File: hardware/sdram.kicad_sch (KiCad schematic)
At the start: 2 parts, among them U1 ECP5U_12_CABGA256, U7 W9825G6KH

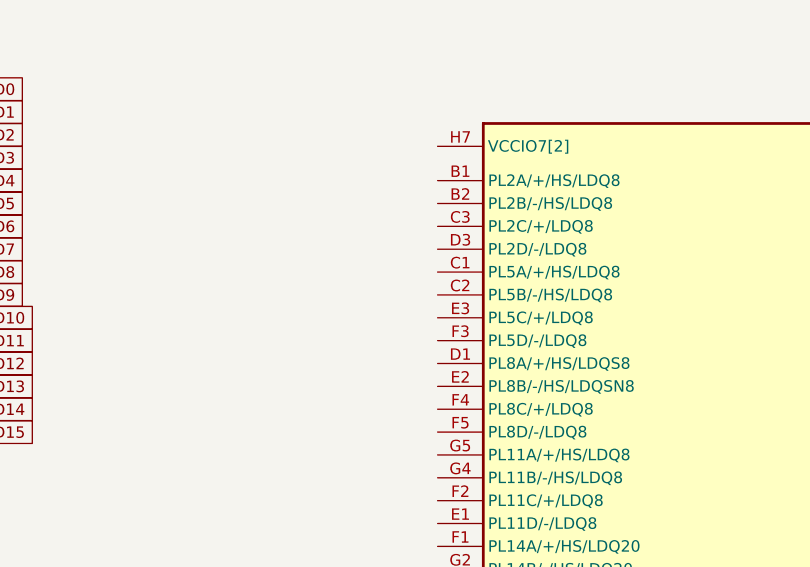
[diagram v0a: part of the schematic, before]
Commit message: Routed most of sdram
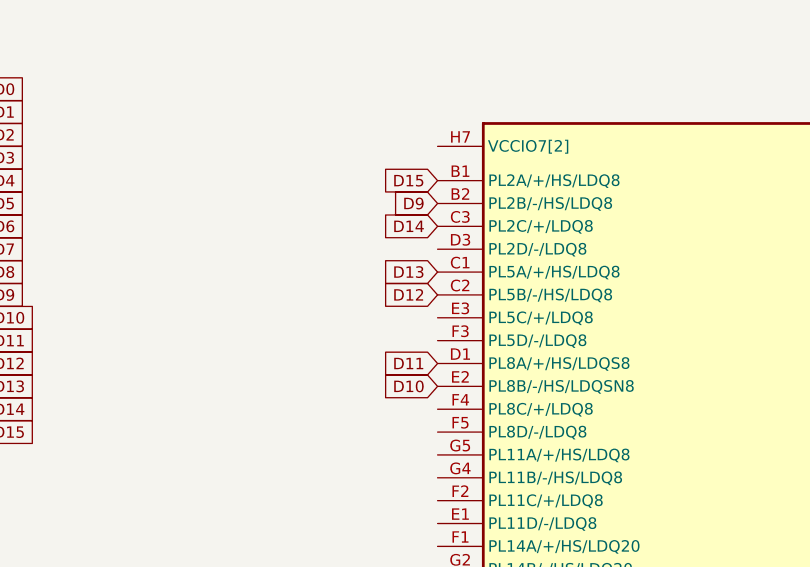
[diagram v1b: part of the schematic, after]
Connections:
- net D10: now also U1.E2 (PL8B/-/HS/LDQSN8)
- net D11: now also U1.D1 (PL8A/+/HS/LDQS8)
- net D12: now also U1.C2 (PL5B/-/HS/LDQ8)
- net D13: now also U1.C1 (PL5A/+/HS/LDQ8)
- net D14: now also U1.C3 (PL2C/+/LDQ8)
- net D15: now also U1.B1 (PL2A/+/HS/LDQ8)
- net D9: now also U1.B2 (PL2B/-/HS/LDQ8)
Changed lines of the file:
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@@
+		)
+	)
+	(global_label "D13"
+		(shape input)
+		(at 113.03 58.42 180)
+		(fields_autoplaced yes)
+		(effects
+			(font
+				(size 1.27 1.27)
+			)
+			(justify right)
+		)
+		(property "Intersheetrefs" "${INTERSHEET_REFS}"
+			(at 106.3558 58.42 0)
+			(effects
+				(font
+					(size 1.27 1.27)
+				)
+				(justify right)
+				(hide yes)
+			)
 		)
 	)
@@
 		)
 	)
+	(global_label "D9"
+		(shape input)
+		(at 113.03 50.8 180)
+		(fields_autoplaced yes)
+		(effects
+			(font
+				(size 1.27 1.27)
+			)
+			(justify right)
+		)
+		(property "Intersheetrefs" "${INTERSHEET_REFS}"
+			(at 107.5653 50.8 0)
+			(effects
+				(font
+					(size 1.27 1.27)
+				)
+				(justify right)
+				(hide yes)
+			)
+		)
+	)
 	(global_label "DQM1"
 		(shape input)
@@
 		)
 	)
+	(global_label "D14"
+		(shape input)
+		(at 113.03 53.34 180)
+		(fields_autoplaced yes)
+		(effects
+			(font
+				(size 1.27 1.27)
+			)
+			(justify right)
+		)
+		(property "Intersheetrefs" "${INTERSHEET_REFS}"
+			(at 106.3558 53.34 0)
+			(effects
+				(font
+					(size 1.27 1.27)
+				)
+				(justify right)
+				(hide yes)
+			)
+		)
+	)
+	(global_label "D10"
+		(shape input)
+		(at 113.03 71.12 180)
+		(fields_autoplaced yes)
+		(effects
+			(font
+				(size 1.27 1.27)
+			)
+			(justify right)
+		)
+		(property "Intersheetrefs" "${INTERSHEET_REFS}"
+			(at 106.3558 71.12 0)
+			(effects
+				(font
+					(size 1.27 1.27)
+				)
+				(justify right)
+				(hide yes)
+			)
+		)
+	)
+	(global_label "D15"
+		(shape input)
+		(at 113.03 48.26 180)
+		(fields_autoplaced yes)
+		(effects
+			(font
+				(size 1.27 1.27)
+			)
+			(justify right)
+		)
+		(property "Intersheetrefs" "${INTERSHEET_REFS}"
+			(at 106.3558 48.26 0)
+			(effects
+				(font
+					(size 1.27 1.27)
+				)
+				(justify right)
+				(hide yes)
+			)
+		)
+	)
 	(global_label "D2"
 		(shape input)
@@
 		)
 	)
+	(global_label "D11"
+		(shape input)
+		(at 113.03 68.58 180)
+		(fields_autoplaced yes)
+		(effects
+			(font
+				(size 1.27 1.27)
+			)
+			(justify right)
+		)
+		(property "Intersheetrefs" "${INTERSHEET_REFS}"
+			(at 106.3558 68.58 0)
+			(effects
+				(font
+					(size 1.27 1.27)
+				)
+				(justify right)
+				(hide yes)
+			)
+		)
+	)
 	(global_label "A10"
 		(shape input)
@@
 		(property "Intersheetrefs" "${INTERSHEET_REFS}"
 			(at 31.5467 48.26 0)
+			(effects
+				(font
+					(size 1.27 1.27)
+				)
+				(justify right)
+				(hide yes)
+			)
+		)
+	)
+	(global_label "D12"
+		(shape input)
+		(at 113.03 60.96 180)
+		(fields_autoplaced yes)
+		(effects
+			(font
+				(size 1.27 1.27)
+			)
+			(justify right)
+		)
+		(property "Intersheetrefs" "${INTERSHEET_REFS}"
+			(at 106.3558 60.96 0)
 			(effects
 				(font
@@
 			)
 		)
-		(property "Datasheet" ""
+		(property "Datasheet" "https://www.lcsc.com/datasheet/lcsc_datasheet_2411220131_Lattice-LFE5U-25F-6BG256C_C1521614.pdf"
 			(at 116.84 43.18 0)
 			(effects

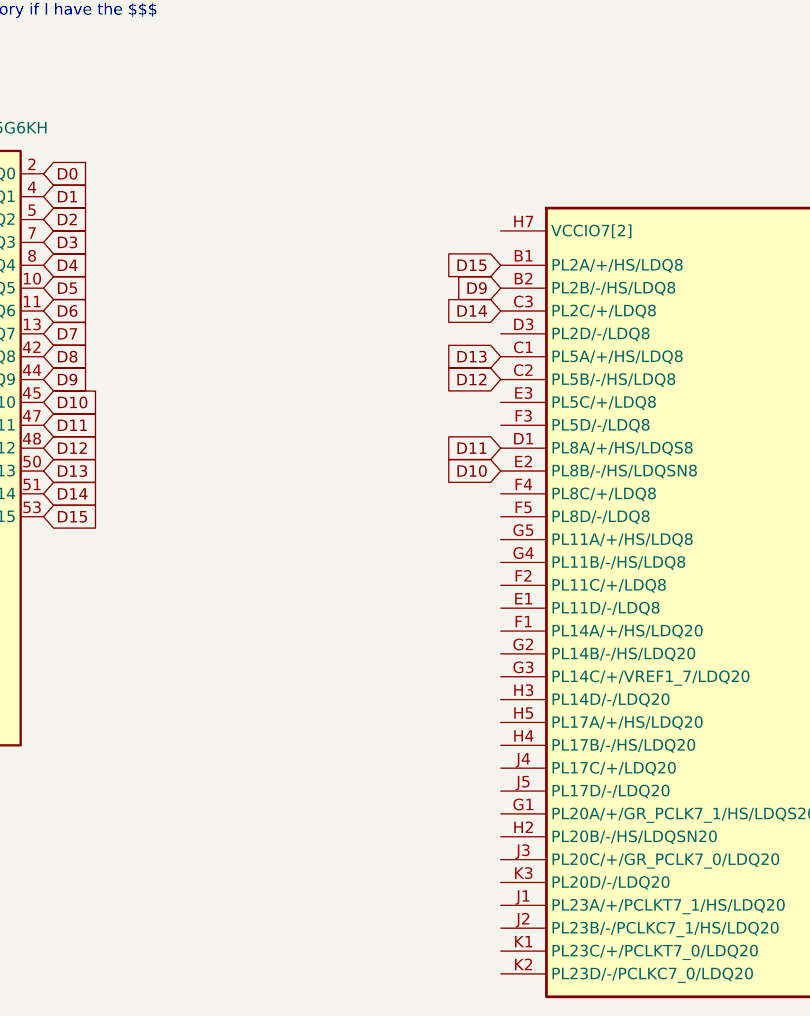
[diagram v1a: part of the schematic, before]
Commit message: Added the decoupling capacitors
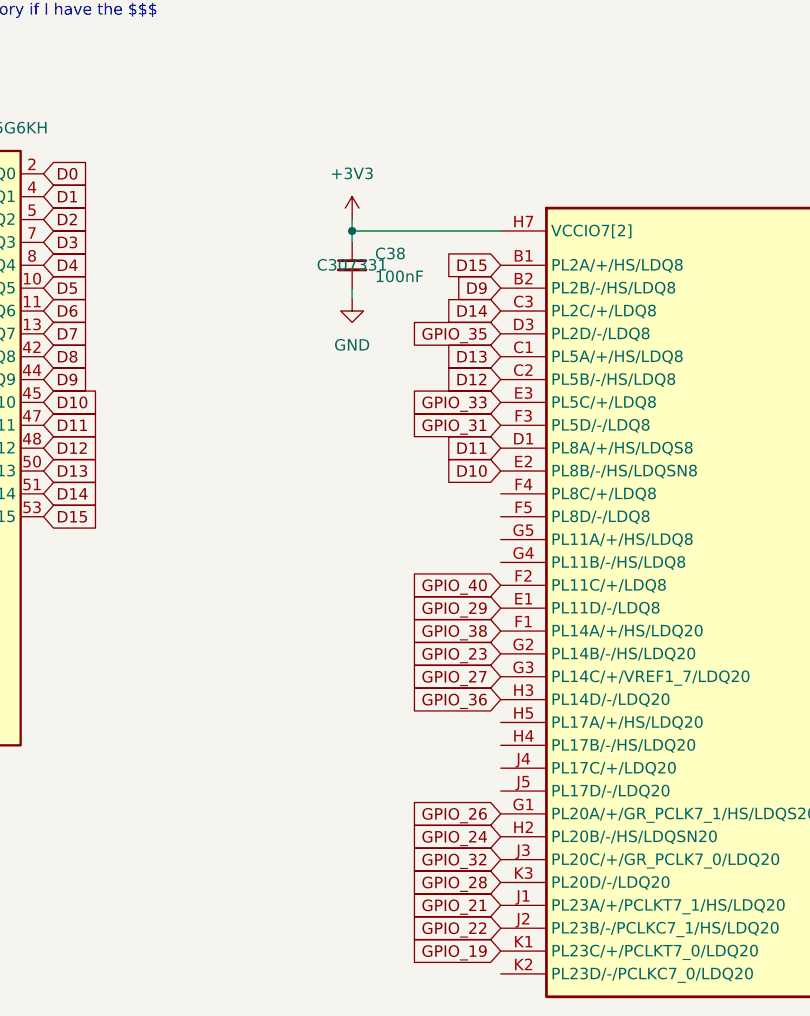
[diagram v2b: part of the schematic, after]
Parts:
- added C38: 100nF, Capacitor_SMD:C_0402_1005Metric, symbol Device:C_Small
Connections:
- net +3V3: now also U1.H6 (VCCIO7[2]), U1.H7 (VCCIO7[2]), C38.1
- net GND: now also C38.2
- net GPIO_35: now reaches U1.D3 (PL2D/-/LDQ8)
- net GPIO_29: now reaches U1.E1 (PL11D/-/LDQ8)
- net GPIO_33: now reaches U1.E3 (PL5C/+/LDQ8)
- net GPIO_38: now reaches U1.F1 (PL14A/+/HS/LDQ20)
- net GPIO_40: now reaches U1.F2 (PL11C/+/LDQ8)
- net GPIO_31: now reaches U1.F3 (PL5D/-/LDQ8)
- net GPIO_26: now reaches U1.G1 (PL20A/+/GR_PCLK7_1/HS/LDQS20)
- net GPIO_23: now reaches U1.G2 (PL14B/-/HS/LDQ20)
- net GPIO_27: now reaches U1.G3 (PL14C/+/VREF1_7/LDQ20)
- net GPIO_24: now reaches U1.H2 (PL20B/-/HS/LDQSN20)
- net GPIO_36: now reaches U1.H3 (PL14D/-/LDQ20)
- net GPIO_21: now reaches U1.J1 (PL23A/+/PCLKT7_1/HS/LDQ20)
- net GPIO_22: now reaches U1.J2 (PL23B/-/PCLKC7_1/HS/LDQ20)
- net GPIO_32: now reaches U1.J3 (PL20C/+/GR_PCLK7_0/LDQ20)
- net GPIO_19: now reaches U1.K1 (PL23C/+/PCLKT7_0/LDQ20)
- net GPIO_28: now reaches U1.K3 (PL20D/-/LDQ20)

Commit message: V1.0 Final Revision and Readme documentation
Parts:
- removed C38: 100nF, Capacitor_SMD:C_0402_1005Metric, symbol Device:C_Small
- removed U1: ECP5U_12_CABGA256, Package_BGA:BGA-256_14.0x14.0mm_Layout16x16_P0.8mm_Ball0.45mm_Pad0.32mm_NSMD, symbol josh:ECP5U_12_CABGA256
- added C30, C31, C32, C34, C35: 100nF, Capacitor_SMD:C_0402_1005Metric, symbol Device:C_Small
- added C33: 10uF, Capacitor_SMD:C_0603_1608Metric, symbol Device:C_Small
- renumbered U7 to U10
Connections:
- net +3V3: now also C30.1, C31.1, C32.1, C33.1, C34.1, C35.1
- net GND: now also C30.2, C31.2, C32.2, C33.2, C34.2, C35.2
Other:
- moved on the sheet: U10

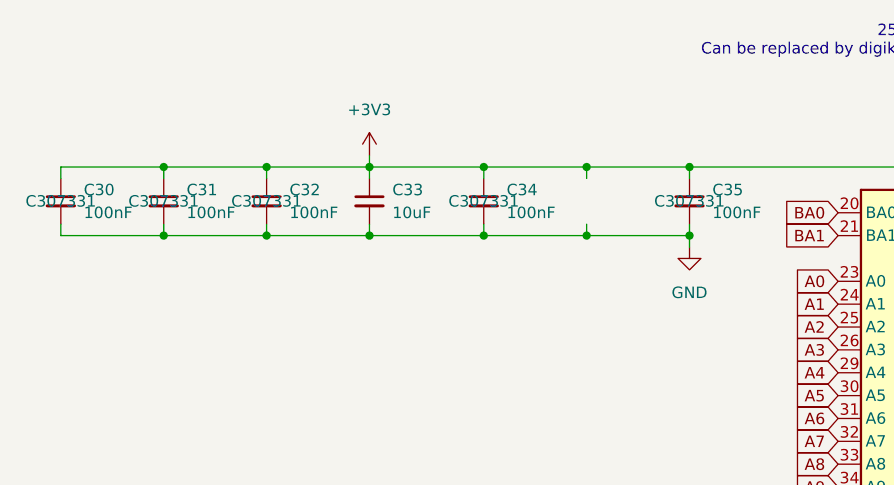
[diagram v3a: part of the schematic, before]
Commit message: Fix level shifter EN voltage error
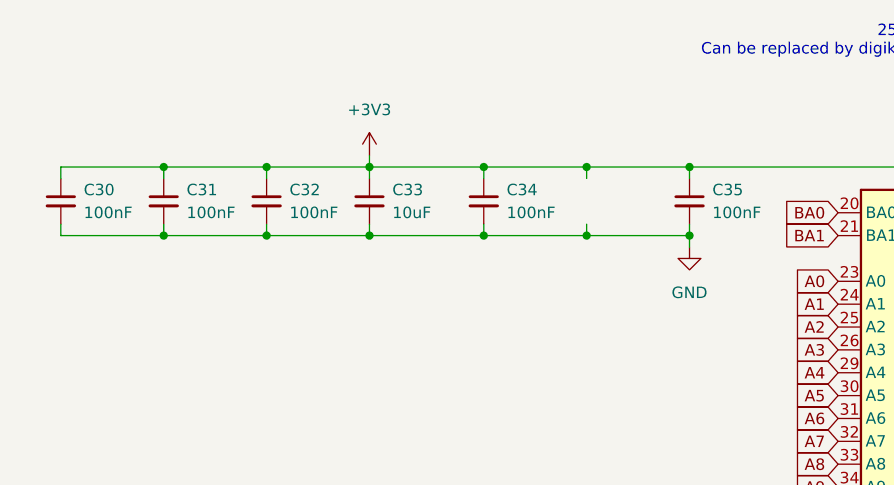
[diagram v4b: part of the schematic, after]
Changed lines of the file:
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@@
 					(size 1.27 1.27)
 				)
+				(hide yes)
 			)
 		)
@@
 					(size 1.27 1.27)
 				)
+				(hide yes)
 			)
 		)
@@
 					(size 1.27 1.27)
 				)
+				(hide yes)
 			)
 		)
@@
 					(size 1.27 1.27)
 				)
+				(hide yes)
 			)
 		)
@@
 					(size 1.27 1.27)
 				)
-			)
-		)
+				(hide yes)
+			)
+		)

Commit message: Pre-prod fixes
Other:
- moved on the sheet: C30, C31, C32, C33, C34, C35

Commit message: Final revision
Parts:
- C30, C31, C32, C34, C35: JLCPCB Part # C307331 -> (none); LCSC Part # (none) -> C307331
- U10: JLCPCB Part # C62246 -> (none); LCSC Part # (none) -> C62246
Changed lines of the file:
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@@
 			)
 		)
-		(property "JLCPCB Part #" "C307331 "
+		(property "LCSC Part #" "C307331 "
 			(at 151.13 53.34 0)
 			(effects
@@
 					(size 1.27 1.27)
 				)
-				(hide yes)
 			)
 		)
@@
 			)
 		)
-		(property "JLCPCB Part #" "C307331 "
+		(property "LCSC Part #" "C307331 "
 			(at 127 53.34 0)
 			(effects
@@
 					(size 1.27 1.27)
 				)
-				(hide yes)
 			)
 		)
@@
 			)
 		)
-		(property "JLCPCB Part #" "C307331 "
+		(property "LCSC Part #" "C307331 "
 			(at 163.83 53.34 0)
 			(effects
@@
 					(size 1.27 1.27)
 				)
-				(hide yes)
 			)
 		)
@@
 			)
 		)
-		(property "JLCPCB Part #" "C62246"
+		(property "LCSC Part #" "C62246"
 			(at 175.26 100.33 0)
 			(effects
@@
 					(size 1.27 1.27)
 				)
-				(hide yes)
 			)
 		)
@@
 			)
 		)
-		(property "JLCPCB Part #" "C307331 "
+		(property "LCSC Part #" "C307331 "
 			(at 115.57 53.34 0)
 			(effects
@@
 					(size 1.27 1.27)
 				)
-				(hide yes)
 			)
 		)
@@
 			)
 		)
-		(property "JLCPCB Part #" "C307331 "
+		(property "LCSC Part #" "C307331 "
 			(at 104.14 53.34 0)
 			(effects
@@
 					(size 1.27 1.27)
 				)
-				(hide yes)
-			)
-		)
+			)
+		)

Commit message: Last checks
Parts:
- C42: renamed from C33; LCSC Part # (none) -> C19702
- renumbered C30 to C39, C31 to C40, C32 to C41, C34 to C43, C35 to C44
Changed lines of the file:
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@@
 	(title_block
 		(title "Icepi zero")
-		(date "2025-05-04")
+		(date "2025-05-12")
 		(rev "v1")
 		(company "Chengyin Yao (cheyao)")
@@
 		(dnp no)
 		(fields_autoplaced yes)
-		(property "Reference" "#PWR057"
+		(property "Reference" "#PWR071"
 			(at 172.72 52.07 0)
 			(effects
@@
 			(project "icepi-zero"
 				(path "/f88da08e-cf42-4d03-a08f-3f602fe6658d/3bffbb9a-e009-498c-a1b0-c490cdf30139"
-					(reference "#PWR057")
+					(reference "#PWR071")
 					(unit 1)
 				)
@@
 		(dnp no)
 		(fields_autoplaced yes)
-		(property "Reference" "C34"
+		(property "Reference" "C43"
 			(at 153.67 52.0762 0)
 			(effects
@@
 					(size 1.27 1.27)
 				)
+				(hide yes)
 			)
 		)
@@
 			(project "icepi-zero"
 				(path "/f88da08e-cf42-4d03-a08f-3f602fe6658d/3bffbb9a-e009-498c-a1b0-c490cdf30139"
-					(reference "C34")
+					(reference "C43")
 					(unit 1)
 				)
@@
 		(dnp no)
 		(fields_autoplaced yes)
-		(property "Reference" "C32"
+		(property "Reference" "C41"
 			(at 129.54 52.0762 0)
 			(effects
@@
 					(size 1.27 1.27)
 				)
+				(hide yes)
 			)
 		)
@@
 			(project "icepi-zero"
 				(path "/f88da08e-cf42-4d03-a08f-3f602fe6658d/3bffbb9a-e009-498c-a1b0-c490cdf30139"
-					(reference "C32")
+					(reference "C41")
 					(unit 1)
 				)
@@
 		(dnp no)
 		(fields_autoplaced yes)
-		(property "Reference" "C35"
+		(property "Reference" "C44"
 			(at 166.37 52.0762 0)
 			(effects
@@
 					(size 1.27 1.27)
 				)
+				(hide yes)
 			)
 		)
@@
 			(project "icepi-zero"
 				(path "/f88da08e-cf42-4d03-a08f-3f602fe6658d/3bffbb9a-e009-498c-a1b0-c490cdf30139"
-					(reference "C35")
+					(reference "C44")
 					(unit 1)
 				)
@@
 					(size 1.27 1.27)
 				)
+				(hide yes)
 			)
 		)
@@
 		(dnp no)
 		(fields_autoplaced yes)
-		(property "Reference" "#PWR060"
+		(property "Reference" "#PWR073"
 			(at 173.99 143.51 0)
 			(effects
@@
 			(project "icepi-zero"
 				(path "/f88da08e-cf42-4d03-a08f-3f602fe6658d/3bffbb9a-e009-498c-a1b0-c490cdf30139"
-					(reference "#PWR060")
+					(reference "#PWR073")
 					(unit 1)
 				)
@@
 		(dnp no)
 		(fields_autoplaced yes)
-		(property "Reference" "C31"
+		(property "Reference" "C40"
 			(at 118.11 52.0762 0)
 			(effects
@@
 					(size 1.27 1.27)
 				)
+				(hide yes)
 			)
 		)
@@
 			(project "icepi-zero"
 				(path "/f88da08e-cf42-4d03-a08f-3f602fe6658d/3bffbb9a-e009-498c-a1b0-c490cdf30139"
-					(reference "C31")
+					(reference "C40")
 					(unit 1)
 				)
@@
 		(dnp no)
 		(fields_autoplaced yes)
-		(property "Reference" "C30"
+		(property "Reference" "C39"
 			(at 106.68 52.0762 0)
 			(effects
@@
 					(size 1.27 1.27)
 				)
+				(hide yes)
 			)
 		)
@@
 			(project "icepi-zero"
 				(path "/f88da08e-cf42-4d03-a08f-3f602fe6658d/3bffbb9a-e009-498c-a1b0-c490cdf30139"
-					(reference "C30")
+					(reference "C39")
 					(unit 1)
 				)
@@
 		(dnp no)
 		(fields_autoplaced yes)
-		(property "Reference" "#PWR059"
+		(property "Reference" "#PWR072"
 			(at 163.83 64.77 0)
 			(effects
@@
 			(project "icepi-zero"
 				(path "/f88da08e-cf42-4d03-a08f-3f602fe6658d/3bffbb9a-e009-498c-a1b0-c490cdf30139"
-					(reference "#PWR059")
+					(reference "#PWR072")
 					(unit 1)
 				)
@@
 		(dnp no)
 		(fields_autoplaced yes)
-		(property "Reference" "C33"
+		(property "Reference" "C42"
 			(at 140.97 52.0762 0)
 			(effects
@@
 		)
 		(property "Description" "Unpolarized capacitor, small symbol"
+			(at 138.43 53.34 0)
+			(effects
+				(font
+					(size 1.27 1.27)
+				)
+				(hide yes)
+			)
+		)
+		(property "LCSC Part #" "C19702"
 			(at 138.43 53.34 0)
 			(effects
@@
 			(project "icepi-zero"
 				(path "/f88da08e-cf42-4d03-a08f-3f602fe6658d/3bffbb9a-e009-498c-a1b0-c490cdf30139"
-					(reference "C33")
+					(reference "C42")
 					(unit 1)
 				)
